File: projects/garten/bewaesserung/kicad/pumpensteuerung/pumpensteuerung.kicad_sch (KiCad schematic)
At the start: 6 parts, among them J2 Screw_Terminal_01x02

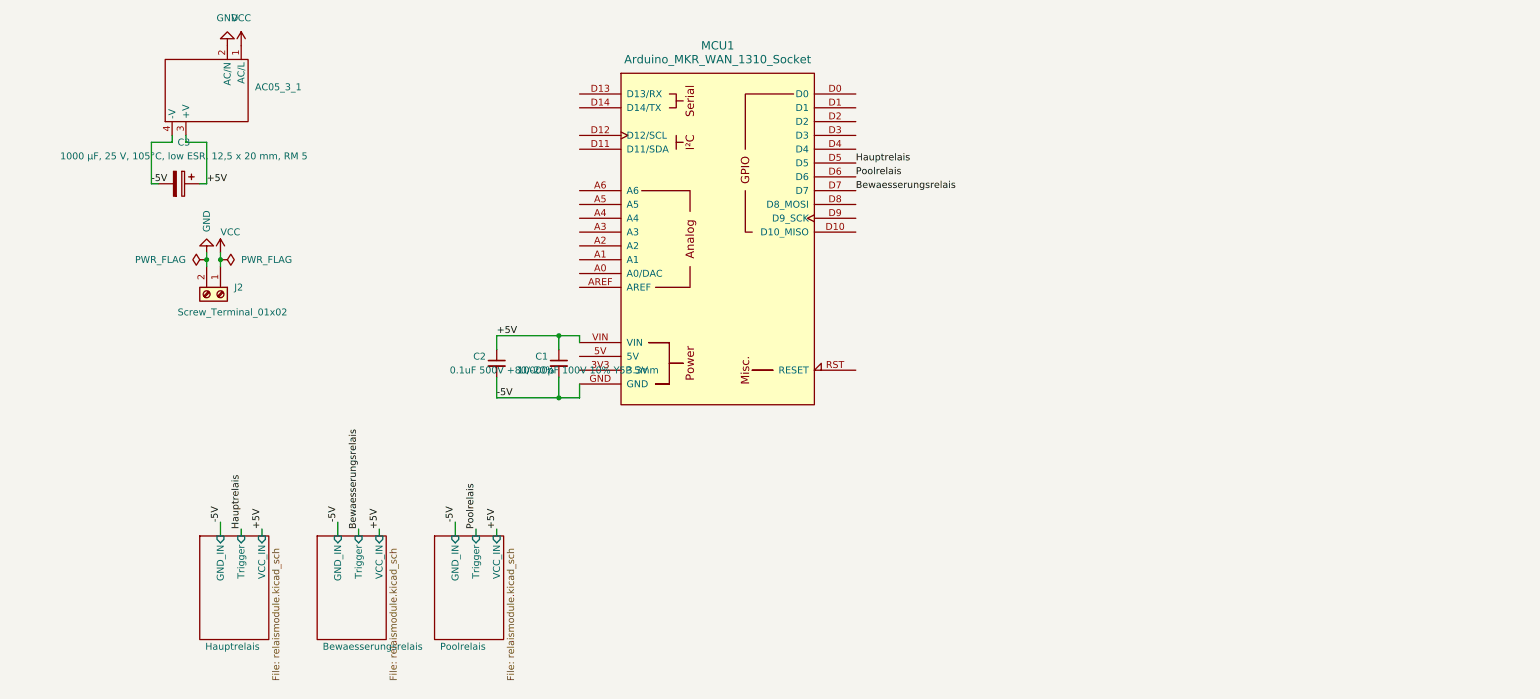
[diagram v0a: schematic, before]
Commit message: [garten/bewaesserung] change powersupply from 230VAC to 24VDC
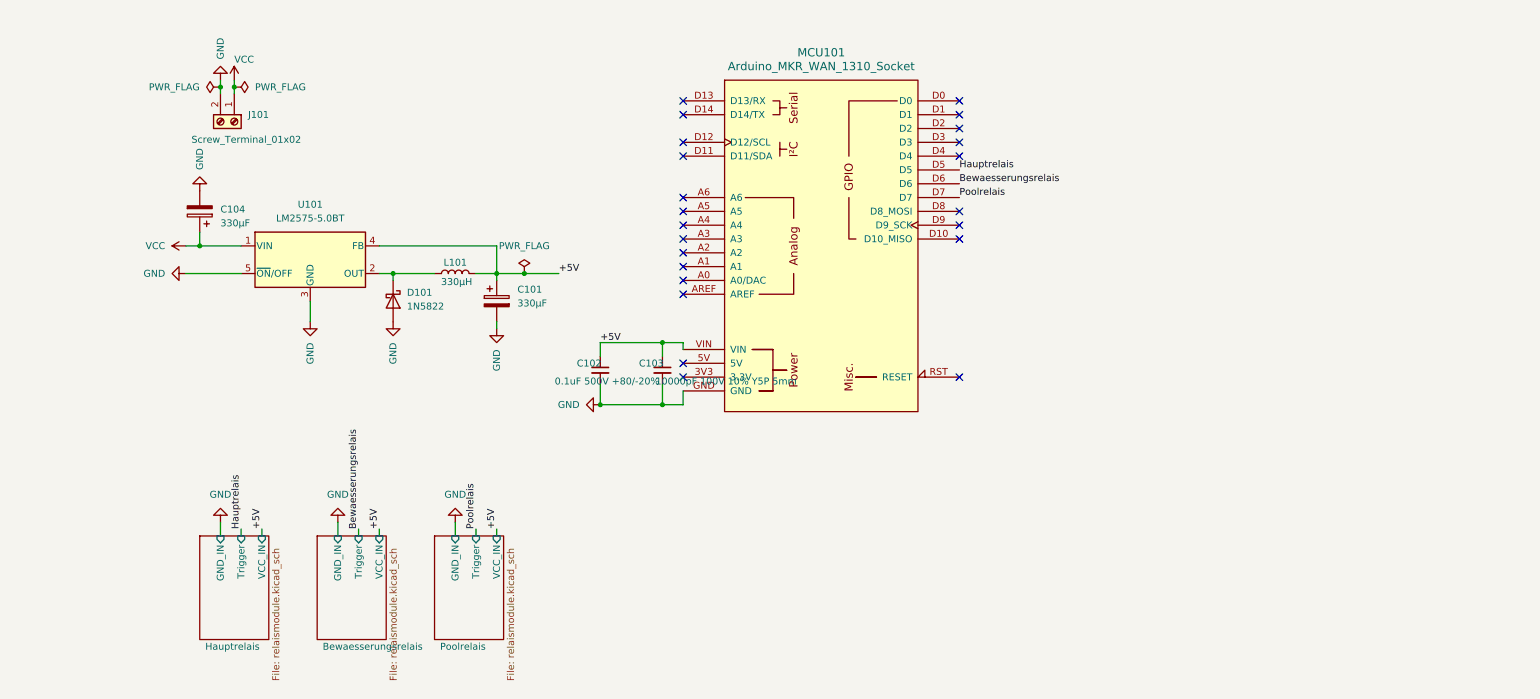
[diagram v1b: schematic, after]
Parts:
- removed AC05_3_1: ~, AZFootprints:AZ_PSU_Module, symbol AZ-Delivery:AC-05-3
- removed C3: 1000 µF, 25 V, 105°C, low ESR, 12,5 x 20 mm, RM 5, Capacitor_THT:CP_Radial_D12.5mm_P5.00mm, symbol Device:C_Polarized
- added C101, C104: 330µF, Capacitor_THT:CP_Radial_D8.0mm_P2.50mm, symbol Device:C_Polarized
- added D101: 1N5822, Diode_THT:D_DO-201AD_P15.24mm_Horizontal, symbol Diode:1N5822
- added L101: 330µH, Inductor_THT:L_Radial_D8.7mm_P5.00mm_Fastron_07HCP, symbol Device:L
- added U101: LM2575-5.0BT, Package_TO_SOT_THT:TO-220-5_Vertical, symbol Regulator_Switching:LM2575-5.0BT
- renumbered C2 to C102, C1 to C103, J2 to J101, MCU1 to MCU101
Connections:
- net -5V is gone; now on net GND: C102.2, C103.2, MCU101.GND
- net +5V: now also C101.1, L101.2, U101.4 (FB)
- net Bewaesserungsrelais: now also MCU101.D6; no longer MCU101.D7
- net GND: now also C101.2, C104.2, D101.2 (A), U101.3 (GND), U101.5 (~{ON}/OFF)
- net Poolrelais: now also MCU101.D7; no longer MCU101.D6
- net VCC: now also C104.1, U101.1 (VIN)
- new net: D101.1 (K), L101.1, U101.2 (OUT)
- no-connect marks 0 -> 23
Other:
- moved on the sheet: C102, C103, J101, MCU101

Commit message: [garten/bewaesserung(pcb)] add another realy to disable poolfilling
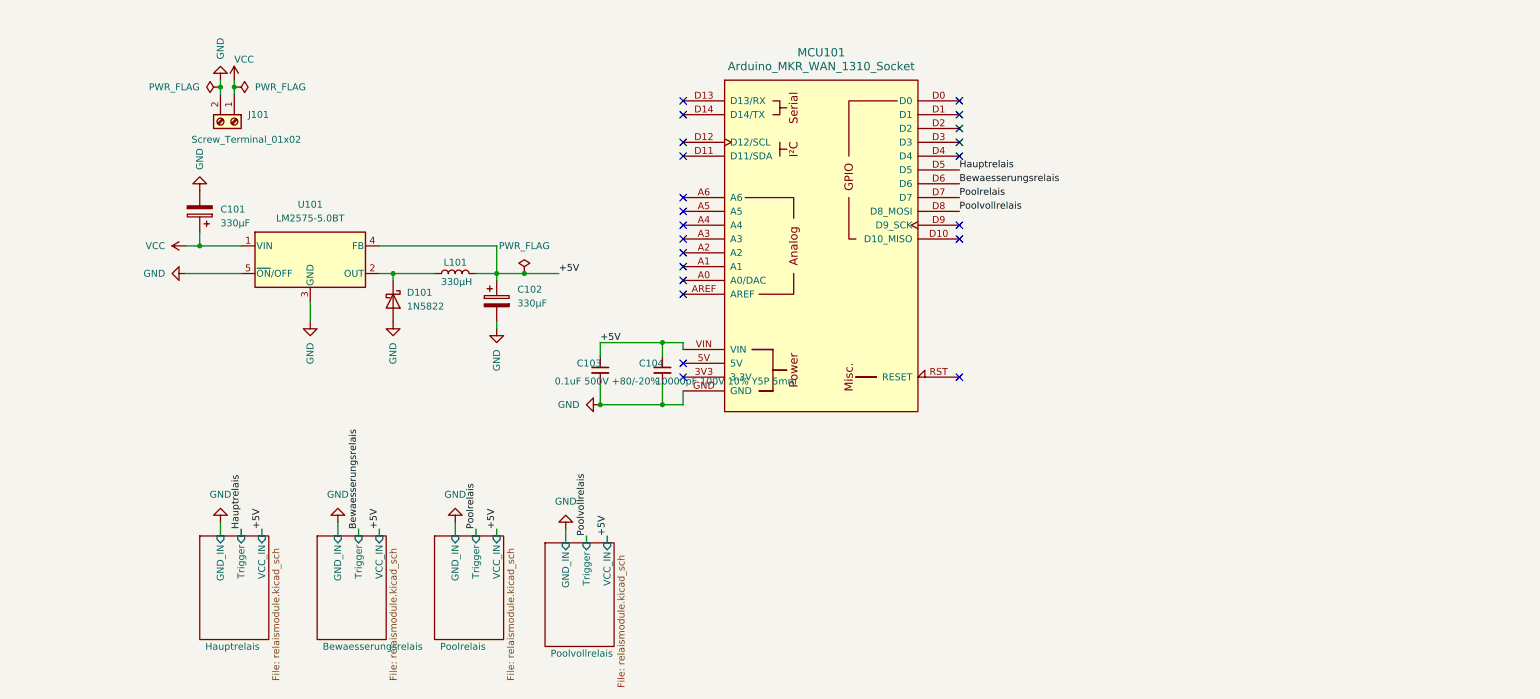
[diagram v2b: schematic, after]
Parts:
- renumbered C104 to C101, C101 to C102, C102 to C103, C103 to C104
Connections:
- net Poolvollrelais: now reaches MCU101.D8 (D8_MOSI)
- no-connect marks 23 -> 22
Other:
- added sheet Poolvollrelais (relaismodule.kicad_sch)
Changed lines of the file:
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@@
-	)
-	(no_connect
-		(at 165.1 48.26)
 	)
 	(no_connect
@@
 	(wire
 		(pts
+			(xy 92.71 106.68) (xy 92.71 109.22)
+		)
+		(stroke
+			(width 0)
+			(type default)
+		)
+	)
+	(wire
+		(pts
 			(xy 80.01 60.96) (xy 80.01 59.69)
 		)
@@
 	(wire
 		(pts
+			(xy 96.52 107.95) (xy 96.52 109.22)
+		)
+		(stroke
+			(width 0)
+			(type default)
+		)
+	)
+	(wire
+		(pts
 			(xy 76.2 59.69) (xy 80.01 59.69)
 		)
@@
 		(pts
 			(xy 114.3 73.66) (xy 114.3 72.39)
+		)
+		(stroke
+			(width 0)
+			(type default)
+		)
+	)
+	(wire
+		(pts
+			(xy 100.33 107.95) (xy 100.33 109.22)
 		)
 		(stroke
@@
 		)
 	)
+	(label "Poolvollrelais"
+		(at 165.1 48.26 0)
+		(effects
+			(font
+				(size 1.27 1.27)
+			)
+			(justify left bottom)
+		)
+	)
+	(label "Poolvollrelais"
+		(at 96.52 107.95 90)
+		(effects
+			(font
+				(size 1.27 1.27)
+			)
+			(justify left bottom)
+		)
+	)
 	(label "+5V"
 		(at 58.42 106.68 90)
@@
 		)
 	)
+	(label "+5V"
+		(at 100.33 107.95 90)
+		(effects
+			(font
+				(size 1.27 1.27)
+			)
+			(justify left bottom)
+		)
+	)
 	(label "Poolrelais"
 		(at 76.2 106.68 90)
@@
 		(dnp no)
 		(fields_autoplaced yes)
-		(property "Reference" "#PWR0109"
+		(property "Reference" "#PWR0112"
 			(at 72.39 99.06 0)
 			(effects
@@
 			(project ""
 				(path "/21a07dfa-371b-4773-840e-44a8dfeac208"
-					(reference "#PWR0109")
+					(reference "#PWR0112")
 					(unit 1)
 				)
@@
 		(on_board yes)
 		(dnp no)
-		(property "Reference" "C103"
+		(property "Reference" "C104"
 			(at 106.172 76.2 0)
 			(effects
@@
 			(project ""
 				(path "/21a07dfa-371b-4773-840e-44a8dfeac208"
-					(reference "C103")
+					(reference "C104")
 					(unit 1)
 				)
@@
 		(on_board yes)
 		(dnp no)
-		(property "Reference" "#PWR0104"
+		(property "Reference" "#PWR0105"
 			(at 16.51 59.69 0)
 			(effects
@@
 			(project "pumpensteuerung"
 				(path "/21a07dfa-371b-4773-840e-44a8dfeac208"
-					(reference "#PWR0104")
+					(reference "#PWR0105")
 					(unit 1)
 				)
@@
 		(on_board yes)
 		(dnp no)
-		(property "Reference" "#PWR0112"
+		(property "Reference" "#PWR0103"
 			(at 25.4 38.1 0)
 			(effects
@@
 			(project "pumpensteuerung"
 				(path "/21a07dfa-371b-4773-840e-44a8dfeac208"
-					(reference "#PWR0112")
+					(reference "#PWR0103")
 					(unit 1)
 				)
@@
 		(dnp no)
 		(fields_autoplaced yes)
-		(property "Reference" "#PWR0108"
+		(property "Reference" "#PWR0109"
 			(at 92.71 83.82 0)
 			(effects
@@
 			(project ""
 				(path "/21a07dfa-371b-4773-840e-44a8dfeac208"
-					(reference "#PWR0108")
+					(reference "#PWR0109")
 					(unit 1)
 				)
@@
 		(on_board yes)
 		(dnp no)
-		(property "Reference" "C102"
+		(property "Reference" "C103"
 			(at 94.742 76.2 0)
 			(effects
@@
 			(project ""
 				(path "/21a07dfa-371b-4773-840e-44a8dfeac208"
-					(reference "C102")
+					(reference "C103")
 					(unit 1)
 				)
@@
 		(dnp no)
 		(fields_autoplaced yes)
-		(property "Reference" "C104"
+		(property "Reference" "C101"
 			(at 29.21 47.8789 0)
 			(effects
@@
 			(project "pumpensteuerung"
 				(path "/21a07dfa-371b-4773-840e-44a8dfeac208"
-					(reference "C104")
+					(reference "C101")
 					(unit 1)
 				)
@@
 		(on_board yes)
 		(dnp no)
-		(property "Reference" "#PWR0107"
+		(property "Reference" "#PWR0108"
 			(at 80.01 76.2 0)
 			(effects
@@
 			(project "pumpensteuerung"
 				(path "/21a07dfa-371b-4773-840e-44a8dfeac208"
-					(reference "#PWR0107")
+					(reference "#PWR0108")
 					(unit 1)
 				)
@@
 		(dnp no)
 		(fields_autoplaced yes)
-		(property "Reference" "#PWR0110"
+		(property "Reference" "#PWR0111"
 			(at 50.8 99.06 0)
 			(effects
@@
 			(project ""
 				(path "/21a07dfa-371b-4773-840e-44a8dfeac208"
-					(reference "#PWR0110")
+					(reference "#PWR0111")
+					(unit 1)
+				)
+			)
+		)
+	)
+	(symbol
+		(lib_id "power:GND")
+		(at 92.71 106.68 180)
+		(unit 1)
+		(exclude_from_sim no)
+		(in_bom yes)
+		(on_board yes)
+		(dnp no)
+		(fields_autoplaced yes)
+		(property "Reference" "#PWR0113"
+			(at 92.71 100.33 0)
+			(effects
+				(font
+					(size 1.27 1.27)
+				)
+				(hide yes)
+			)
+		)
+		(property "Value" "GND"
+			(at 92.71 101.6 0)
+			(effects
+				(font
+					(size 1.27 1.27)
+				)
+			)
+		)
+		(property "Footprint" ""
+			(at 92.71 106.68 0)
+			(effects
+				(font
+					(size 1.27 1.27)
+				)
+				(hide yes)
+			)
+		)
+		(property "Datasheet" ""
+			(at 92.71 106.68 0)
+			(effects
+				(font
+					(size 1.27 1.27)
+				)
+				(hide yes)
+			)
+		)
+		(property "Description" "Power symbol creates a global label with name \"GND\" , ground"
+			(at 92.71 106.68 0)
+			(effects
+				(font
+					(size 1.27 1.27)
+				)
+				(hide yes)
+			)
+		)
+		(pin "1"
+		)
+		(instances
+			(project "pumpensteuerung"
+				(path "/21a07dfa-371b-4773-840e-44a8dfeac208"
+					(reference "#PWR0113")
 					(unit 1)
 				)
@@
 		(dnp no)
 		(fields_autoplaced yes)
-		(property "Reference" "C101"
+		(property "Reference" "C102"
 			(at 83.82 62.6109 0)
 			(effects
@@
 			(project ""
 				(path "/21a07dfa-371b-4773-840e-44a8dfeac208"
-					(reference "C101")
+					(reference "C102")
 					(unit 1)
 				)
@@
 		(on_board yes)
 		(dnp no)
-		(property "Reference" "#PWR0105"
+		(property "Reference" "#PWR0106"
 			(at 45.72 74.93 0)
 			(effects
@@
 			(project "pumpensteuerung"
 				(path "/21a07dfa-371b-4773-840e-44a8dfeac208"
-					(reference "#PWR0105")
+					(reference "#PWR0106")
 					(unit 1)
 				)
@@
 		(on_board yes)
 		(dnp no)
-		(property "Reference" "#PWR0106"
+		(property "Reference" "#PWR0107"
 			(at 60.96 74.93 0)
 			(effects
@@
 			(project "pumpensteuerung"
 				(path "/21a07dfa-371b-4773-840e-44a8dfeac208"
-					(reference "#PWR0106")
+					(reference "#PWR0107")
 					(unit 1)
 				)
@@
 		(on_board yes)
 		(dnp no)
-		(property "Reference" "#PWR0103"
+		(property "Reference" "#PWR0104"
 			(at 26.67 54.61 0)
 			(effects
@@
 			(project "pumpensteuerung"
 				(path "/21a07dfa-371b-4773-840e-44a8dfeac208"
-					(reference "#PWR0103")
+					(reference "#PWR0104")
 					(unit 1)
 				)
@@
 		(dnp no)
 		(fields_autoplaced yes)
-		(property "Reference" "#PWR0111"
+		(property "Reference" "#PWR0110"
 			(at 29.21 99.06 0)
 			(effects
@@
 			(project ""
 				(path "/21a07dfa-371b-4773-840e-44a8dfeac208"
-					(reference "#PWR0111")
+					(reference "#PWR0110")
 					(unit 1)
 				)
@@
 				)
 			)
+		)
+	)
+	(sheet
+		(at 88.9 109.22)
+		(size 12.7 19.05)
+		(exclude_from_sim no)
+		(in_bom yes)
+		(on_board yes)
+		(dnp no)
+		(stroke
+			(width 0.1524)
+			(type solid)
+		)
+		(fill
+			(color 255 229 191 1.0000)
+		)
+		(property "Sheetname" "Poolvollrelais"
+			(at 89.916 130.302 0)
+			(effects
+				(font
+					(size 1.27 1.27)
+				)
+				(justify left bottom)
+			)
+		)
+		(property "Sheetfile" "relaismodule.kicad_sch"
+			(at 102.1846 135.89 90)
+			(effects
+				(font
+					(size 1.27 1.27)
+				)
+				(justify left top)
+			)
+		)
+		(pin "Trigger" input
+			(at 96.52 109.22 90)
+			(effects
+				(font
+					(size 1.27 1.27)
+				)
+				(justify right)
+			)
+		)
+		(pin "VCC_IN" input
+			(at 100.33 109.22 90)
+			(effects
+				(font
+					(size 1.27 1.27)
+				)
+				(justify right)
+			)
+		)
+		(pin "GND_IN" input
+			(at 92.71 109.22 90)
+			(effects
+				(font
+					(size 1.27 1.27)
+				)
+				(justify right)
+			)
+		)
+		(instances
+			(project "pumpensteuerung"
+				(path "/21a07dfa-371b-4773-840e-44a8dfeac208"
+					(page "5")
+				)
+			)

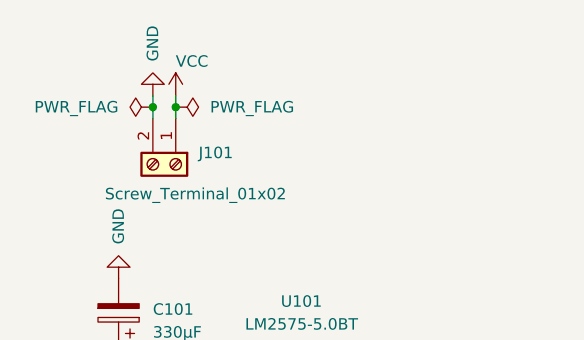
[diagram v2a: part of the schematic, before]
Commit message: [garten/bewaesserung(pcb)] rotate powersupply connector
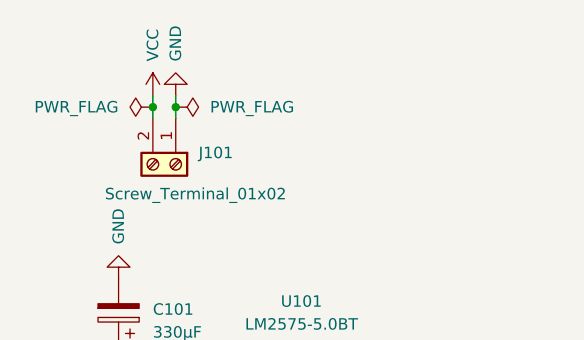
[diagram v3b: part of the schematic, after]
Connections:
- net GND: now also J101.1 (Pin_1); no longer J101.2 (Pin_2)
- net VCC: now also J101.2 (Pin_2); no longer J101.1 (Pin_1)
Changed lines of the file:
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@@
 	(symbol
 		(lib_id "power:GND")
-		(at 29.21 24.13 180)
+		(at 31.75 24.13 180)
 		(unit 1)
 		(exclude_from_sim no)
@@
 		(dnp no)
 		(property "Reference" "#PWR0101"
-			(at 29.21 17.78 0)
+			(at 31.75 17.78 0)
 			(effects
 				(font
@@
 		)
 		(property "Value" "GND"
-			(at 29.2099 20.32 90)
+			(at 31.7499 20.32 90)
 			(effects
 				(font
@@
 		)
 		(property "Footprint" ""
-			(at 29.21 24.13 0)
+			(at 31.75 24.13 0)
 			(effects
 				(font
@@
 		)
 		(property "Datasheet" ""
-			(at 29.21 24.13 0)
+			(at 31.75 24.13 0)
 			(effects
 				(font
@@
 		)
 		(property "Description" "Power symbol creates a global label with name \"GND\" , ground"
-			(at 29.21 24.13 0)
-			(effects
-				(font
-					(size 1.27 1.27)
-				)
-				(hide yes)
-			)
-		)
-		(pin "1"
-		)
-		(instances
-			(project ""
+			(at 31.75 24.13 0)
+			(effects
+				(font
+					(size 1.27 1.27)
+				)
+				(hide yes)
+			)
+		)
+		(pin "1"
+		)
+		(instances
+			(project "pumpensteuerung"
 				(path "/21a07dfa-371b-4773-840e-44a8dfeac208"
 					(reference "#PWR0101")
@@
 	(symbol
 		(lib_id "power:VCC")
-		(at 31.75 24.13 0)
+		(at 29.21 24.13 0)
 		(unit 1)
 		(exclude_from_sim no)
@@
 		(dnp no)
 		(property "Reference" "#PWR0102"
-			(at 31.75 27.94 0)
+			(at 29.21 27.94 0)
 			(effects
 				(font
@@
 		)
 		(property "Value" "VCC"
-			(at 31.7501 20.32 0)
+			(at 29.2101 20.32 90)
 			(effects
 				(font
@@
 		)
 		(property "Footprint" ""
-			(at 31.75 24.13 0)
+			(at 29.21 24.13 0)
 			(effects
 				(font
@@
 		)
 		(property "Datasheet" ""
-			(at 31.75 24.13 0)
+			(at 29.21 24.13 0)
 			(effects
 				(font
@@
 		)
 		(property "Description" "Power symbol creates a global label with name \"VCC\""
-			(at 31.75 24.13 0)
-			(effects
-				(font
-					(size 1.27 1.27)
-				)
-				(hide yes)
-			)
-		)
-		(pin "1"
-		)
-		(instances
-			(project ""
+			(at 29.21 24.13 0)
+			(effects
+				(font
+					(size 1.27 1.27)
+				)
+				(hide yes)
+			)
+		)
+		(pin "1"
+		)
+		(instances
+			(project "pumpensteuerung"
 				(path "/21a07dfa-371b-4773-840e-44a8dfeac208"
 					(reference "#PWR0102")
